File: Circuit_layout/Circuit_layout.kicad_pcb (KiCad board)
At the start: 2 copper layers, 177.8 x 127 mm, 193 parts, among them CON1 AVR-JTAG-10, J1 Spare_Conns, J4 Motor_Ctrl, J5 RJ12, P1 TSV, P2 CONN_02X10, P3 CONN_02X07, Q1 ZVP4525G, Q2 MMBF170, Q3 MMBF170, SW1 SW_PUSH, SW2 TS5A3159-Q1, SW3 JS202011CQN, U1 PDM2-S24-S12, U10 MCP2551-I/SN, U11 TLP293, U12 TLP293, U13 PDQ10-D, U14 Mounting_hole, U15 Mounting_hole, U16 LTC3638, U17 MCP6004, U18 TS912, U19 ACPL-C870, U2 MCP6002, U20 ACPL-C870, U21 MCP6001, U22 TS372, U23 TLP293, U24 TLP293, U25 Mounting_hole, U26 Mounting_hole, U27 TLP293, U3 MCP6004, U4 LM95071-Q1, U5 LM7810CT, U6 TS912, U7 AT90CAN128-A, U8 74ACT11030, U9 TLP293, Y1 10MHz

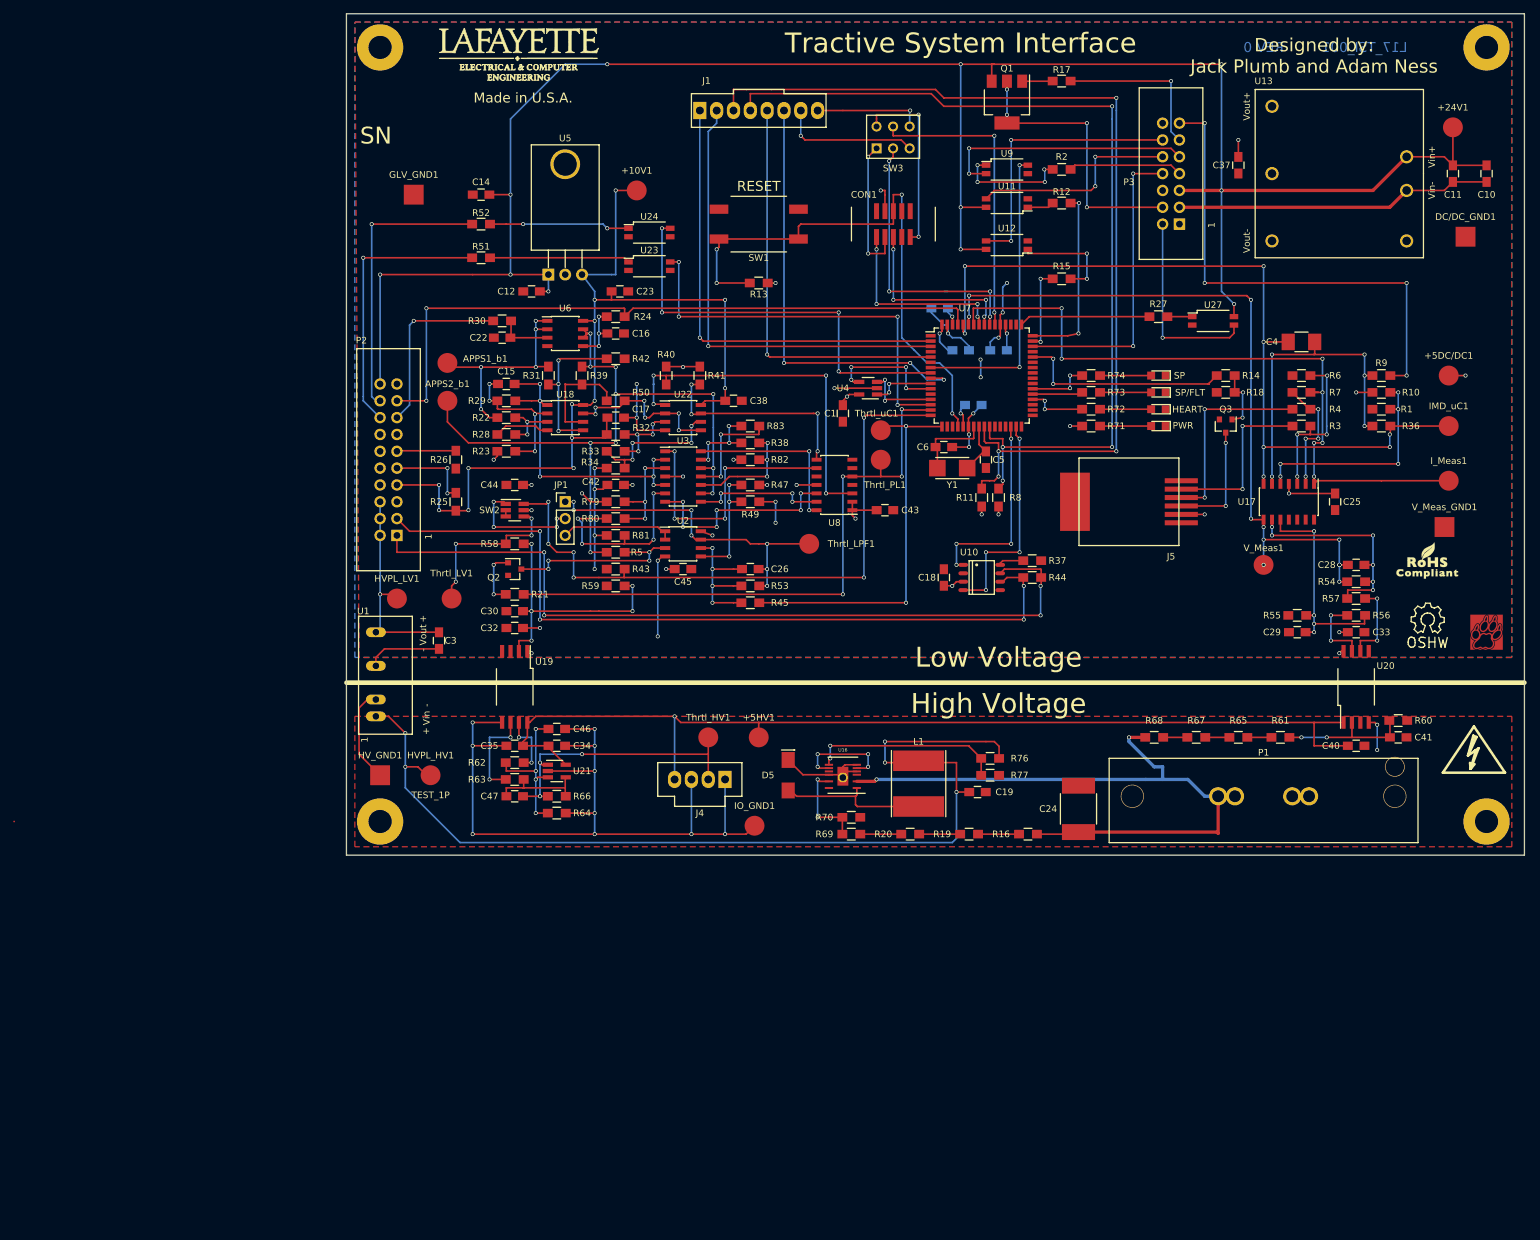
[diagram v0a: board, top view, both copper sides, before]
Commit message: Pots connected, just need to fit regulator on
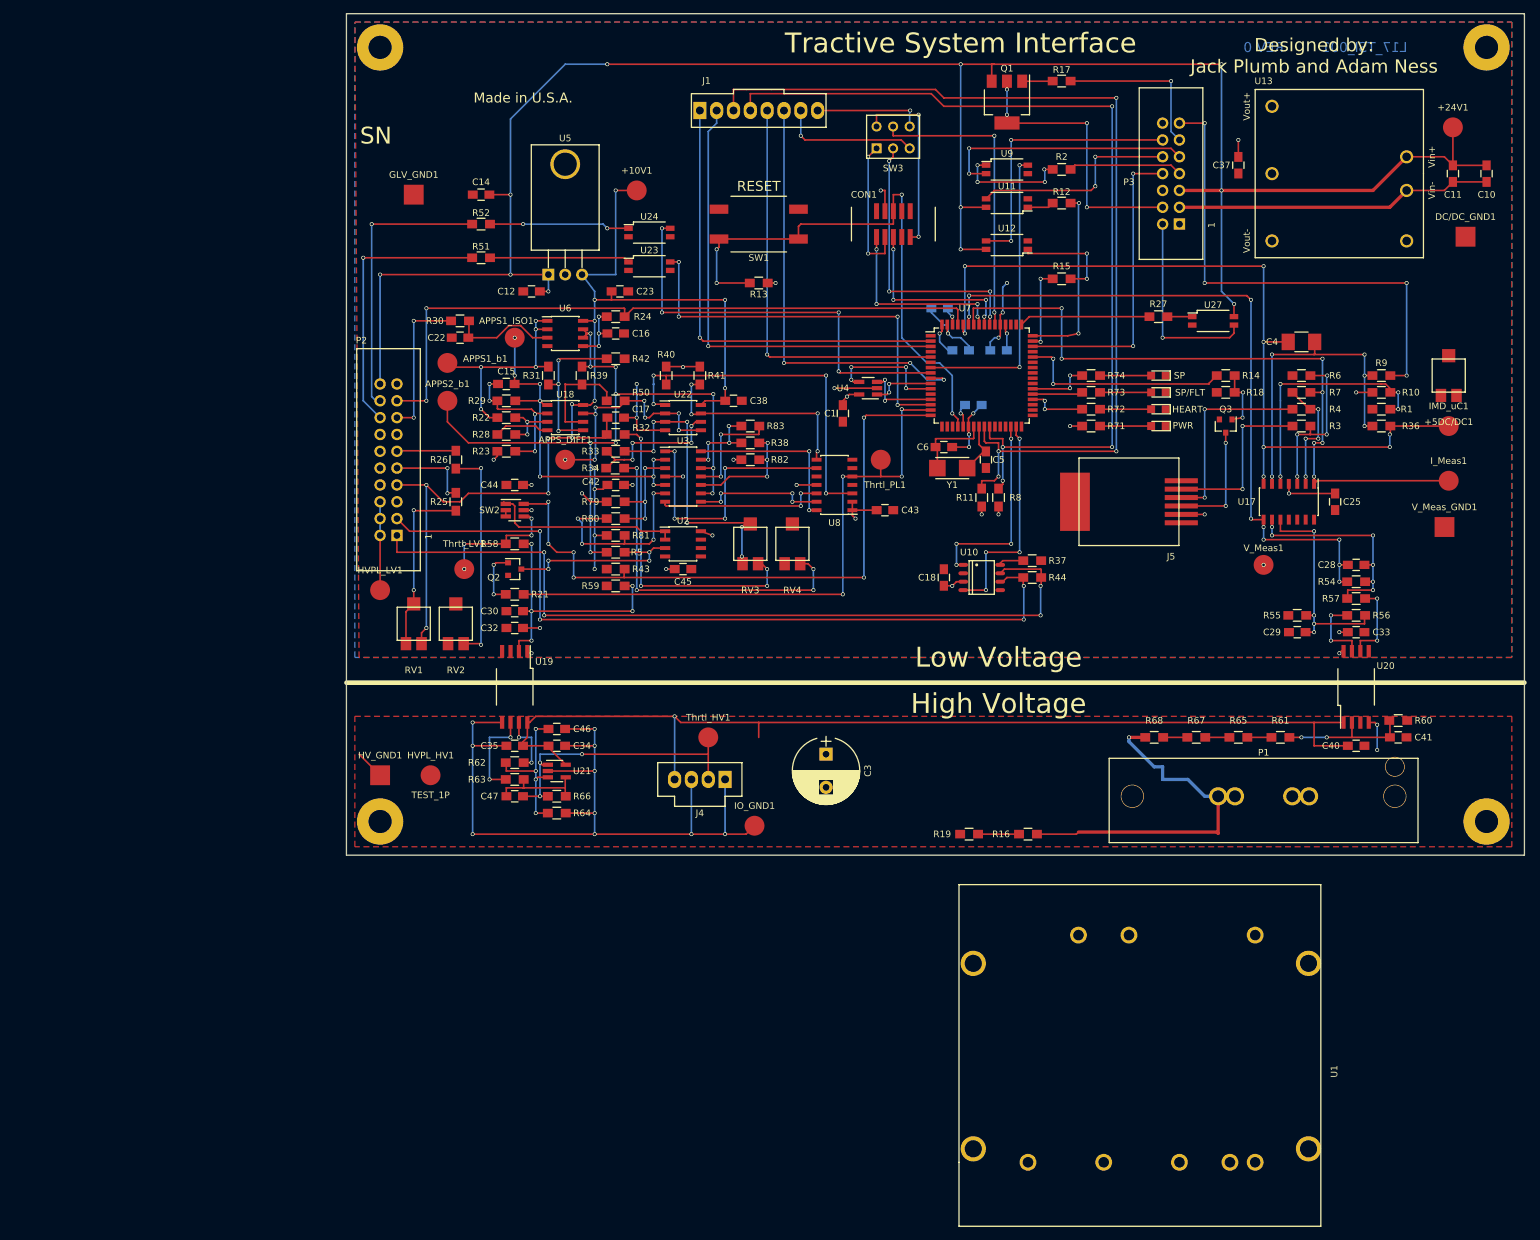
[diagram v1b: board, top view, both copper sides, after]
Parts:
- removed +5HV1: +5HV, Measurement_Points:Measurement_Point_Round-SMD-Pad_Big
- removed ?: , custom_footprints:Symbol_HighVoltage_Type2_FSilk_VerySmall
- removed ?: , custom_footprints:Symbol_HighVoltage_Type2_BSilk_VerySmall
- removed C19: 10uF, Capacitors_SMD:C_0805_HandSoldering
- removed C24: 1uF, Capacitors_SMD:C_2220_HandSoldering
- removed C26: 0.1u, Capacitors_SMD:C_0805_HandSoldering
- removed D5: D_Schottky, custom_footprints:do214ac
- removed G***: LOGO, custom_footprints:logo_lafayette_ece_24mmx9mm
- removed G***: LOGO, custom_footprints:ROHS
- removed JP1: JUMPER3, Pin_Headers:Pin_Header_Straight_1x03_Pitch2.54mm
- removed L1: 100uH, Inductors:Inductor_Taiyo-Yuden_NR-80xx_HandSoldering
- removed R20, R69: 250k, Resistors_SMD:R_0805_HandSoldering
- removed R45, R47, R49, R53: 16k, Resistors_SMD:R_0805_HandSoldering
- removed R70: 47k, Resistors_SMD:R_0805_HandSoldering
- removed R76: 750k, Resistors_SMD:R_0805_HandSoldering
- removed R77: 196k, Resistors_SMD:R_0805_HandSoldering
- removed REF**: Symbol_OSHW-Logo_SilkScreen, custom_footprints:Symbol_OSHW-Logo_SilkScreen
- removed Thrtl_LPF1: Throttle_LPF, Measurement_Points:Measurement_Point_Round-SMD-Pad_Big
- removed Thrtl_uC1: Throttle_uC, Measurement_Points:Measurement_Point_Round-SMD-Pad_Big
- removed U16: LTC3638, custom_footprints:TSSOP16_LTC3638
- removed VAL: REF, custom_footprints:lafLogo
- added APPS1_ISO1: APPS1_ISO, Measurement_Points:Measurement_Point_Round-SMD-Pad_Big, F.Cu at (55.9, 78.1)
- added APPS_DIFF1: APPS_DIFF, Measurement_Points:Measurement_Point_Round-SMD-Pad_Big, F.Cu at (63.5, 96.5)
- added RV1: 2k, custom_footprints:trim_pot, F.Cu at (40.6, 121.3)
- added RV2: 2k, custom_footprints:trim_pot, F.Cu at (47.0, 121.3)
- added RV3: 2k, custom_footprints:trim_pot, F.Cu at (91.4, 109.2)
- added RV4: 2k, custom_footprints:trim_pot, F.Cu at (97.8, 109.2)
- +5DC/DC1: footprint Measurement_Points:Measurement_Point_Round-SMD-Pad_Big -> custom_footprints:trim_pot
- C3: value 2.2uF -> 10uF; footprint Capacitors_SMD:C_0805_HandSoldering -> Capacitors_THT:CP_Radial_D10.0mm_P5.00mm
- R16: value 250k -> 4.3K
- R25, R26: value 2k -> 4k
- R58: value 24.9k -> 15k
- U1: value PDM2-S24-S12 -> RUW15SL12C; footprint custom_footprints:DCDC-Conv_TRACO_TMR_1-xxxx_Single -> custom_footprints:RUW15
- moved U1 119.2 mm to (133.3, 202.6)
- moved C3 60.9 mm to (102.9, 141.0)
- moved C22 6.35 mm to (47.6, 78.1)
- moved R30 6.35 mm to (47.6, 75.6)
- moved Thrtl_LV1 4.84 mm to (48.3, 113.0)
- moved HVPL_LV1 2.84 mm to (35.6, 116.2)
- moved R34 0.08 mm to (71.0, 97.8), turned to 180 degrees
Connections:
- net /CAN Transceiver/CANRX renamed /CANRX
- net /CAN Transceiver/CANTX renamed /CANTX
- net /Isolators/Throttle_LV renamed /Throttle_LV
- net /Isolators/V_Measure renamed /V_Measure
- net /Status Lights/CC_LED_CTRL renamed /CC_LED_CTRL
- net /Status Lights/D_LED_CTRL renamed /D_LED_CTRL
- net /Status Lights/Heartbeat renamed /Heartbeat
- net /Status Lights/RTDS_CTRL renamed /RTDS_CTRL
- net /Status Lights/Spare_Blue renamed /Spare_Blue
- net /Status Lights/Spare_Red renamed /Spare_Red
- net /ThrottlePlausibility/BOT_uC renamed /BOT_uC
- net /ThrottlePlausibility/BP_uC renamed /BP_uC
- net /ThrottlePlausibility/Throttle_PL renamed /Throttle_PL
- net /ThrottlePlausibility/Throttle_SEL renamed /Throttle_SEL
- C3 pad 1: HVPL -> HV+
- C3 pad 2: CH_GND -> HV-
- HVPL_HV1 pad 1: Net-(C19-Pad1) -> HV+
- R19 pad 1: Net-(R19-Pad1) -> Net-(R16-Pad1)
- R19 pad 2: Net-(R16-Pad1) -> HV-
- R25 pad 2: APPS1_10 -> Net-(R25-Pad2)
- R26 pad 1: CH_GND -> Net-(R26-Pad1)
- R33 pad 2: Net-(R32-Pad1) -> Net-(R33-Pad2)
- R34 pad 1: CH_GND -> Net-(R34-Pad1)
- SW2 pad 1: Net-(JP1-Pad2) -> /ThrottlePlausibility/Pedal_Out
- U1 pad 1: Net-(C19-Pad1) -> Net-(R16-Pad1)
- U1 pad 2: HV- -> Net-(U1-Pad2)
- U1 pad 4: CH_GND -> HV-
- U1 pad 6: HVPL -> Net-(U1-Pad6)
- U22 pad 3: Net-(R32-Pad1) -> Net-(R33-Pad2)
- U7 pad 17: /ThrottlePlausibility/Throttle_uC -> /Throttle_uC
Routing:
- net Net-(C19-Pad1): track 152.1 -> 0.00 mm, vias 5 -> 0
- net /ThrottlePlausibility/Throttle_uC: track 58.4 -> 0.00 mm, vias 2 -> 0
- net Net-(R34-Pad1): track 0.00 -> 52.6 mm, vias 0 -> 4
- net Net-(U2-Pad7): track 51.7 -> 0.47 mm, vias 7 -> 0
- net Net-(R33-Pad2): track 0.00 -> 45.9 mm, vias 0 -> 6
- net HV+: track 103.0 -> 57.4 mm, vias 2 -> 1
- net Net-(R32-Pad1): track 12.8 -> 48.2 mm
- net Net-(R26-Pad1): track 0.00 -> 33.2 mm, vias 0 -> 2
- net CH_GND: track 128.9 -> 97.6 mm, vias 20 -> 16
- net Net-(R76-Pad2): track 29.1 -> 0.00 mm, vias 2 -> 0
- net Net-(R25-Pad2): track 0.00 -> 27.0 mm, vias 0 -> 2
- net Net-(U2-Pad6): track 23.7 -> 0.47 mm, vias 4 -> 0
- net Net-(D5-Pad1): track 22.8 -> 0.00 mm
- net HV-: track 35.1 -> 15.9 mm
- net APPS1_10: track 141.3 -> 160.3 mm, vias 14 -> 13
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
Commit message: Board 1.1 for review
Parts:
- removed HVPL_HV1: TEST_1P, Measurement_Points:Measurement_Point_Round-SMD-Pad_Big
- +5DC/DC1: footprint custom_footprints:trim_pot -> Measurement_Points:Measurement_Point_Round-SMD-Pad_Big
- C3: footprint Capacitors_THT:CP_Radial_D10.0mm_P5.00mm -> Capacitors_SMD:CP_Elec_8x10
- moved HV_GND1 167.0 mm to (202.6, 141.0)
- moved U1 61.6 mm to (153.0, 144.1)
- moved P1 59.9 mm to (109.1, 144.1)
- moved C41 52.8 mm to (136.5, 142.2), turned to 270 degrees
- moved R60 50.6 mm to (139.1, 142.3), turned to 90 degrees
- moved C40 49.0 mm to (134.0, 142.2), turned to 270 degrees
- moved U20 47.0 mm to (135.9, 130.8)
- moved R67 46.8 mm to (114.3, 153.0)
- moved R68 46.8 mm to (108.0, 153.0)
- moved R61 46.8 mm to (127.0, 153.0)
- moved R65 46.8 mm to (120.7, 153.0)
- moved R16 33.7 mm to (99.6, 153.0)
- moved R19 33.7 mm to (90.7, 153.0), turned to 180 degrees
- moved C18 31.5 mm to (89.5, 118.7), turned to 0 degrees
- moved C28 30.5 mm to (200.7, 87.6)
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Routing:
- net HVPL: track 13.3 -> 169.6 mm, vias 2 -> 5
- net CH_GND: track 97.6 -> 234.1 mm, vias 16 -> 27
- net Net-(R57-Pad1): track 12.3 -> 98.3 mm, vias 2 -> 4
- net Net-(R56-Pad1): track 11.1 -> 92.4 mm, vias 2 -> 4
- net HV+: track 57.4 -> 131.3 mm
- net Net-(R16-Pad1): track 0.00 -> 69.2 mm
- net +5HV: track 156.0 -> 108.3 mm, vias 1 -> 2
- net A1_LV: track 26.3 -> 66.5 mm, vias 2 -> 4
- net A2_LV: track 30.1 -> 69.9 mm
- net I_RTN: track 17.8 -> 54.6 mm
- net /CANTX: track 30.3 -> 63.9 mm, vias 4 -> 6
- net /CANRX: track 33.4 -> 67.0 mm, vias 4 -> 6
- net CANL: track 118.9 -> 89.4 mm, vias 4 -> 2
- net +5V: track 82.8 -> 110.6 mm, vias 30 -> 32
- net CANH: track 122.6 -> 95.9 mm, vias 4 -> 2
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
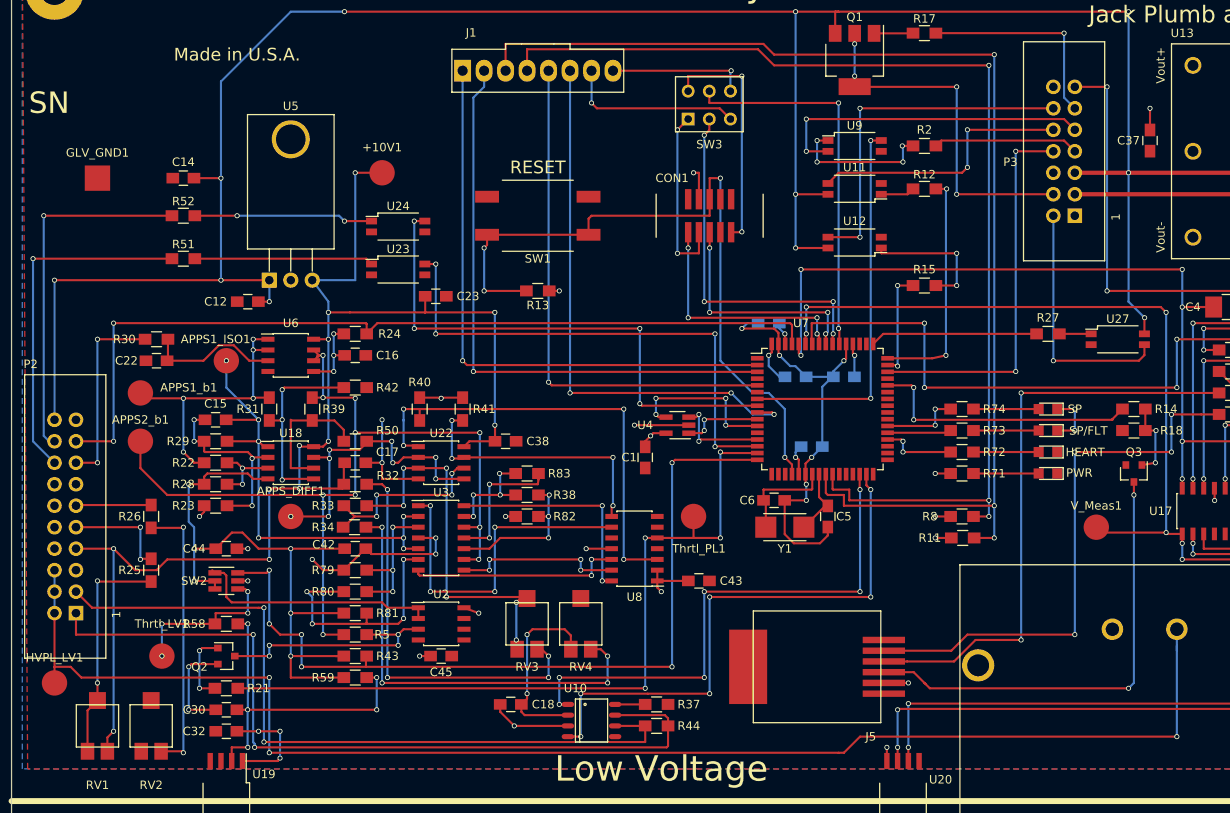
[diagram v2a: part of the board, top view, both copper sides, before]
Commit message: Wider traces for DC/DC converter
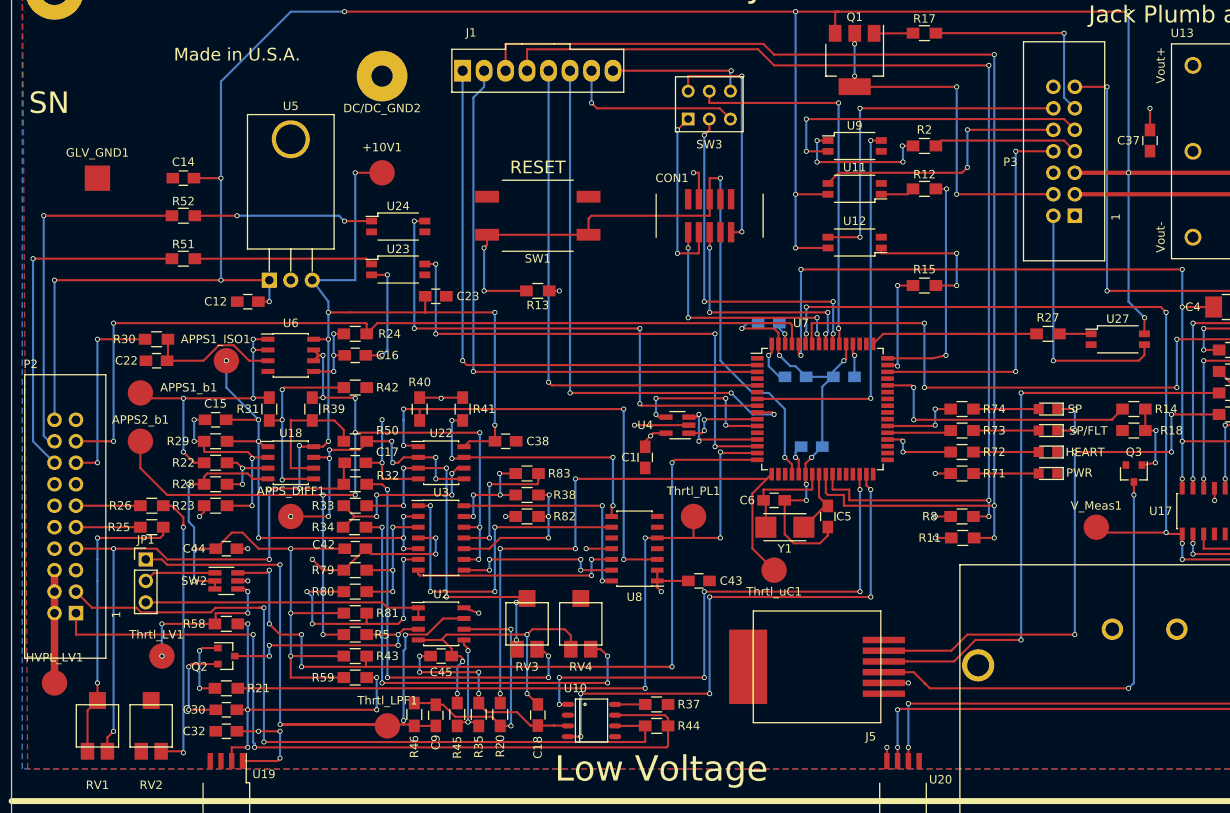
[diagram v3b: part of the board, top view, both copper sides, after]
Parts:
- added C9: 0.1u, Capacitors_SMD:C_0805_HandSoldering, F.Cu at (80.6, 120.0)
- added DC/DC_GND2: +5DC/DC_GND, Wire_Pads:SolderWirePad_single_2-5mmDrill, F.Cu at (74.3, 44.5)
- added JP1: Jumper_NC_Dual, Pin_Headers:Pin_Header_Straight_1x03_Pitch2.54mm, F.Cu at (46.4, 101.6)
- added R20: 16k, Resistors_SMD:R_0805_HandSoldering, F.Cu at (88.3, 119.9)
- added R35: 16k, Resistors_SMD:R_0805_HandSoldering, F.Cu at (85.7, 119.9)
- added R45: 16k, Resistors_SMD:R_0805_HandSoldering, F.Cu at (83.2, 119.9)
- added R46: 16k, Resistors_SMD:R_0805_HandSoldering, F.Cu at (78.1, 119.9)
- added Thrtl_LPF1: Throttle_LPF, Measurement_Points:Measurement_Point_Round-SMD-Pad_Big, F.Cu at (74.9, 121.3)
- added Thrtl_uC1: Throttle_uC, Measurement_Points:Measurement_Point_Round-SMD-Pad_Big, F.Cu at (120.7, 102.9)
- R32, R34: value 4.75k -> 4k
- moved R25 5.08 mm to (47.1, 97.8), turned to 0 degrees
- moved C18 3.43 mm to (92.7, 120.0), turned to 90 degrees
- moved R26 1.27 mm to (47.1, 95.2), turned to 180 degrees
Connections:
- SW2 pad 1: /ThrottlePlausibility/Pedal_Out -> Net-(JP1-Pad2)
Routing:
- net HVPL: track 169.6 -> 13.3 mm, vias 5 -> 0
- net Net-(C9-Pad1): track 0.47 -> 85.3 mm, vias 0 -> 4
- net /Throttle_uC: track 0.00 -> 71.7 mm, vias 0 -> 4
- net CH_GND: track 234.1 -> 264.0 mm, vias 27 -> 31
- net Net-(C9-Pad2): track 0.47 -> 30.1 mm, vias 0 -> 2
- net +5V: track 110.6 -> 125.3 mm, vias 32 -> 34
- net Net-(R35-Pad2): track 0.00 -> 12.8 mm, vias 0 -> 2
- net Net-(JP1-Pad2): track 0.00 -> 8.57 mm
- net Net-(R25-Pad2): track 27.0 -> 34.5 mm
- net APPS2_5: track 12.7 -> 7.62 mm, vias 2 -> 0
- net /ThrottlePlausibility/Pedal_Out: track 29.4 -> 34.2 mm
- net APPS1_RTN: track 8.92 -> 7.73 mm
- net CANL: track 89.4 -> 90.5 mm
- net APPS1_10: track 160.9 -> 159.9 mm
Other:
- net class TSAL added: clearance 0.254, trace_width 0.889, via_dia 0.6, via_drill 0.4
